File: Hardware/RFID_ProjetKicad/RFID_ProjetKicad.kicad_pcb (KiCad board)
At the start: 2 copper layers, 25 parts, among them J1 TB0011-350-04GR, J2 TB0011-350-04GR, U1 XIAO-ESP32-C6-DIP, U2 CEG006900, U3 MAX3485CSA_T

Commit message: Création du PCB
placement, routage et controle
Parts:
- C2, C3, C4, D1, D2, R2, R3, R4, U3: moved to B.Cu
- L2: value 5 mH -> (none)
- moved E2 134.5 mm to (78.0, 176.0), turned to 90 degrees
- moved D1 134.3 mm to (80.0, 156.0), turned to 180 degrees
- moved F1 131.2 mm to (88.7, 169.4), turned to -90 degrees
- moved C3 127.5 mm to (80.0, 169.5), turned to -90 degrees
- moved C4 120.5 mm to (76.0, 163.5)
- moved D2 113.8 mm to (63.0, 136.0)
- moved R1 106.4 mm to (82.5, 176.0), turned to -90 degrees
- moved J1 105.5 mm to (62.0, 176.0)
- moved C2 99.4 mm to (76.5, 138.5), turned to 90 degrees
- moved J2 95.8 mm to (97.2, 176.5)
- moved R2 93.2 mm to (98.0, 167.0), turned to 180 degrees
- moved L2 87.6 mm to (71.8, 137.3)
- moved PS1 84.5 mm to (77.5, 168.0), turned to 180 degrees
- moved L1 72.4 mm to (101.5, 145.5), turned to 180 degrees
- moved C1 65.0 mm to (63.5, 147.9), turned to 90 degrees
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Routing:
- net GND: track 0.00 -> 749.6 mm, vias 0 -> 1
- net +3V3: track 0.00 -> 394.7 mm, vias 0 -> 3
- net Net-(U1-GPIO21_D3): track 0.00 -> 107.0 mm, vias 0 -> 1
- net /D+: track 0.00 -> 106.4 mm, vias 0 -> 2
- net /D-: track 0.00 -> 106.2 mm, vias 0 -> 2
- net Net-(U1-GPIO16_D6_TX): track 0.00 -> 93.4 mm
- net Net-(U1-GPIO0_A0_D0): track 0.00 -> 92.1 mm
- net +7V à 27.6V: track 0.00 -> 92.0 mm
- net Net-(U1-GPIO20_D9_MISO): track 0.00 -> 81.9 mm
- net Net-(U1-GPIO18_D10_MOSI): track 0.00 -> 76.5 mm
- net Net-(U1-GPIO19_D8_SCK): track 0.00 -> 75.4 mm
- net /SW_COM: track 0.00 -> 70.7 mm, vias 0 -> 2
- net Net-(U1-GPIO17_D7_RX): track 0.00 -> 60.6 mm, vias 0 -> 2
- net Net-(C1-Pad1): track 0.00 -> 53.9 mm
- net +8V à 28V: track 0.00 -> 33.3 mm
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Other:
- board outline added: 72 x 151 mm
- board text added: "+"
- board text added: "+8v-28v"
- board text added: "-"
- board text added: "0v"
- board text added: "D+"
- board text added: "D-"
- board text added: "GND"

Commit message: Correction PCB + Logos
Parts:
- added G***: LOGO, RFID_Empreintes:EST_logo_grand, F.Cu at (50.6, 92.7)
- added G***: LOGO, RFID_Empreintes:QR_GitHub_7mm, F.Cu at (49.6, 127.2)
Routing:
- net Net-(U1-GPIO2_A2_D2): track 2.11 -> 59.4 mm, vias 0 -> 2
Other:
- board text added: "RS485"

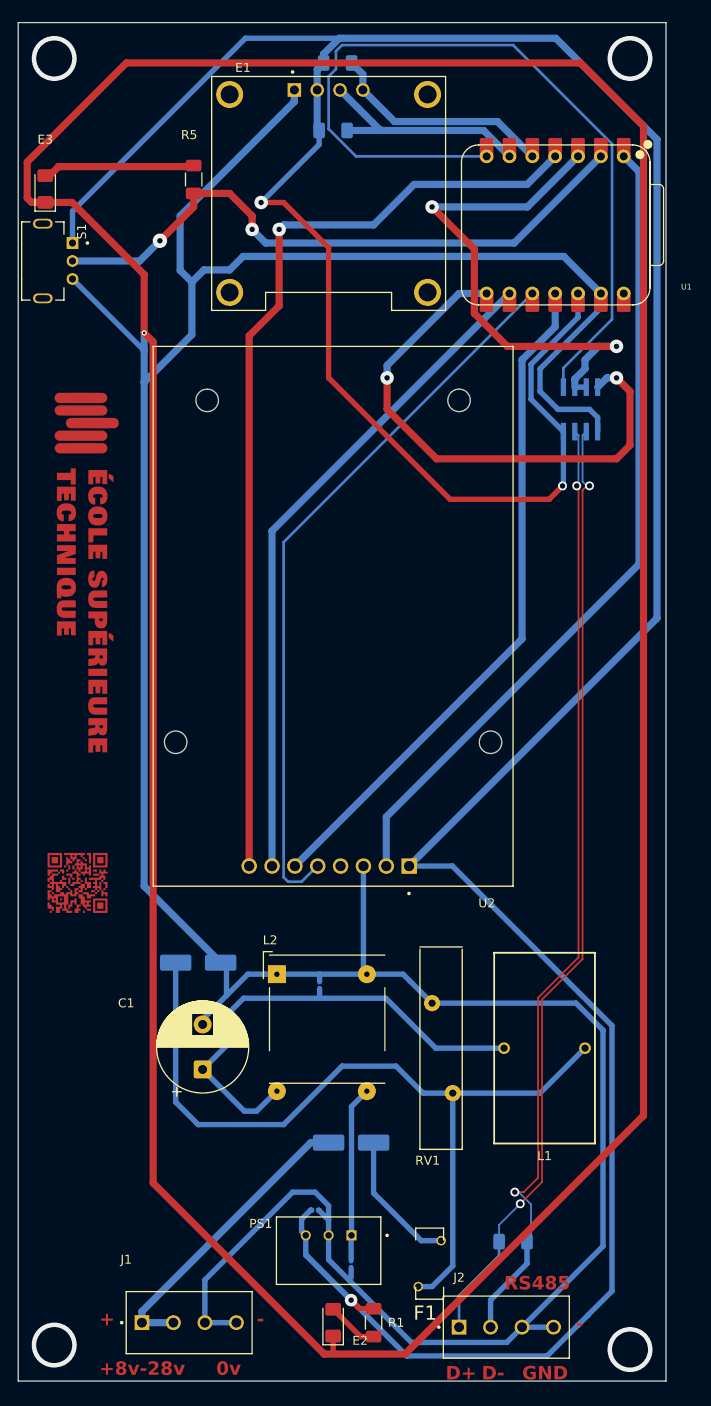
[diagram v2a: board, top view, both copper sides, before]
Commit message: Ajout de points de test sur PCB
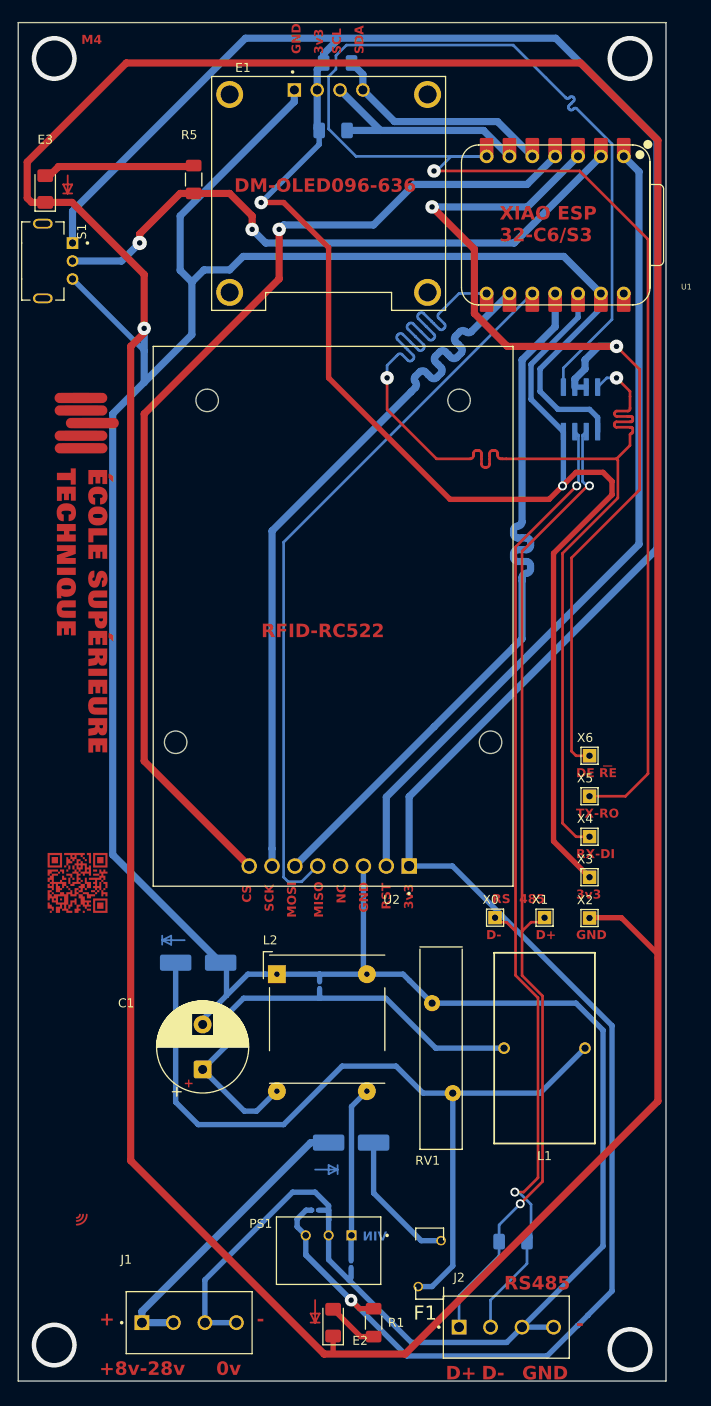
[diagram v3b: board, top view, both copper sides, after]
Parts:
- added X0: , TestPoint:TestPoint_THTPad_1.5x1.5mm_Drill0.7mm, F.Cu at (96.0, 131.0)
- added X1: , TestPoint:TestPoint_THTPad_1.5x1.5mm_Drill0.7mm, F.Cu at (101.5, 131.0)
- added X2: , TestPoint:TestPoint_THTPad_1.5x1.5mm_Drill0.7mm, F.Cu at (106.5, 131.0)
- added X3: , TestPoint:TestPoint_THTPad_1.5x1.5mm_Drill0.7mm, F.Cu at (106.5, 126.5)
- added X4: , TestPoint:TestPoint_THTPad_1.5x1.5mm_Drill0.7mm, F.Cu at (106.5, 122.0)
- added X5: , TestPoint:TestPoint_THTPad_1.5x1.5mm_Drill0.7mm, F.Cu at (106.5, 117.5)
- added X6: , TestPoint:TestPoint_THTPad_1.5x1.5mm_Drill0.7mm, F.Cu at (106.5, 113.0)
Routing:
- net Net-(U1-GPIO16_D6_TX): track 93.4 -> 195.3 mm, vias 0 -> 1
- net Net-(U1-GPIO17_D7_RX): track 60.6 -> 138.2 mm
- net +3V3: track 394.7 -> 450.3 mm
- net Net-(U1-GPIO2_A2_D2): track 59.4 -> 110.8 mm
- net GND: track 749.6 -> 765.4 mm
- net Net-(U1-GPIO21_D3): track 107.0 -> 116.7 mm
- net Net-(U1-GPIO19_D8_SCK): track 75.4 -> 81.8 mm
- net Net-(U1-GPIO18_D10_MOSI): track 76.5 -> 81.8 mm
- net /D+: track 106.4 -> 111.4 mm
- net /D-: track 106.2 -> 111.0 mm
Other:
- board text added: "3v3"
- board text added: "CS"
- board text added: "DE RE"
- board text added: "DM-OLED096-636"
- board text added: "M4"
- board text added: "MISO"
- board text added: "MOSI"
- board text added: "NC"
- board text added: "RFID-RC522"
- board text added: "RS 485"
- board text added: "RST"
- board text added: "RX-DI"
- board text added: "SCK"
- board text added: "SCL"
- board text added: "SDA"
- board text added: "TX-RO"
- board text added: "VIN"
- board text added: "XIAO ESP 32-C6/S3"
- board text added: "_"

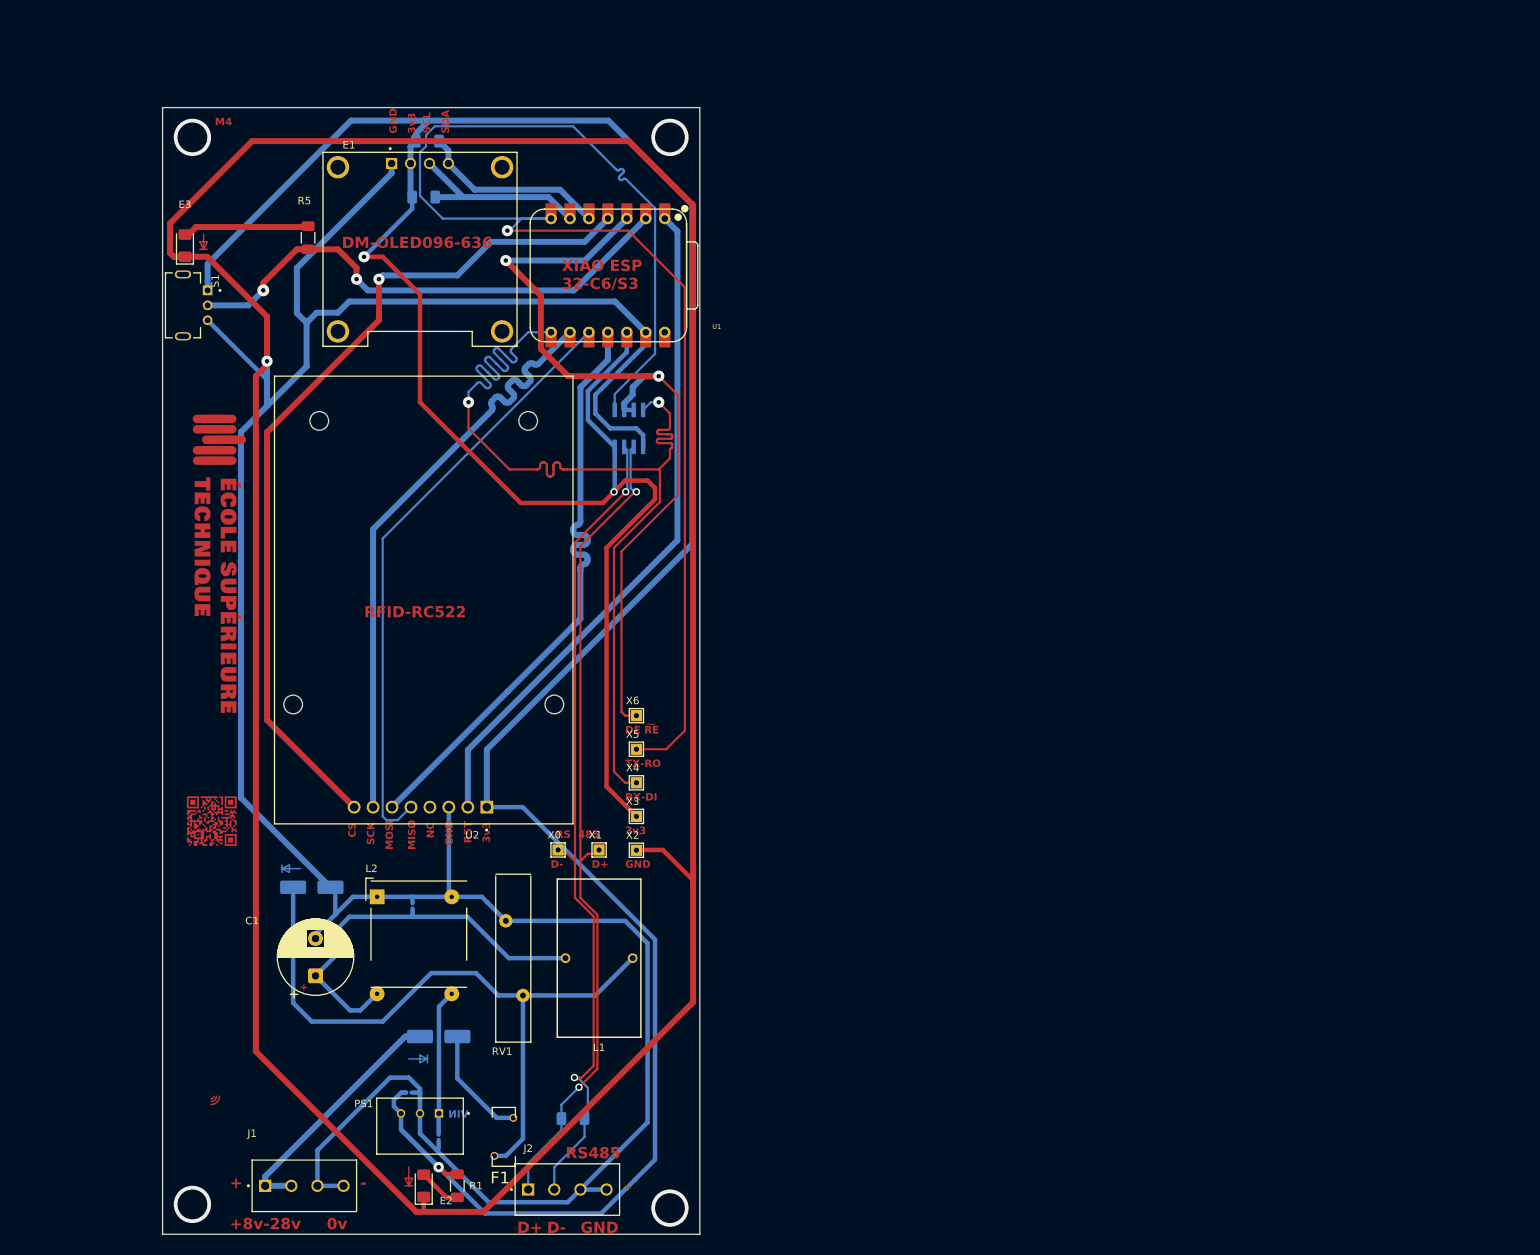
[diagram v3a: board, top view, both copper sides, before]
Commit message: Ajout de la documentation sur l'implémentation PCB + Modification PCB et logos
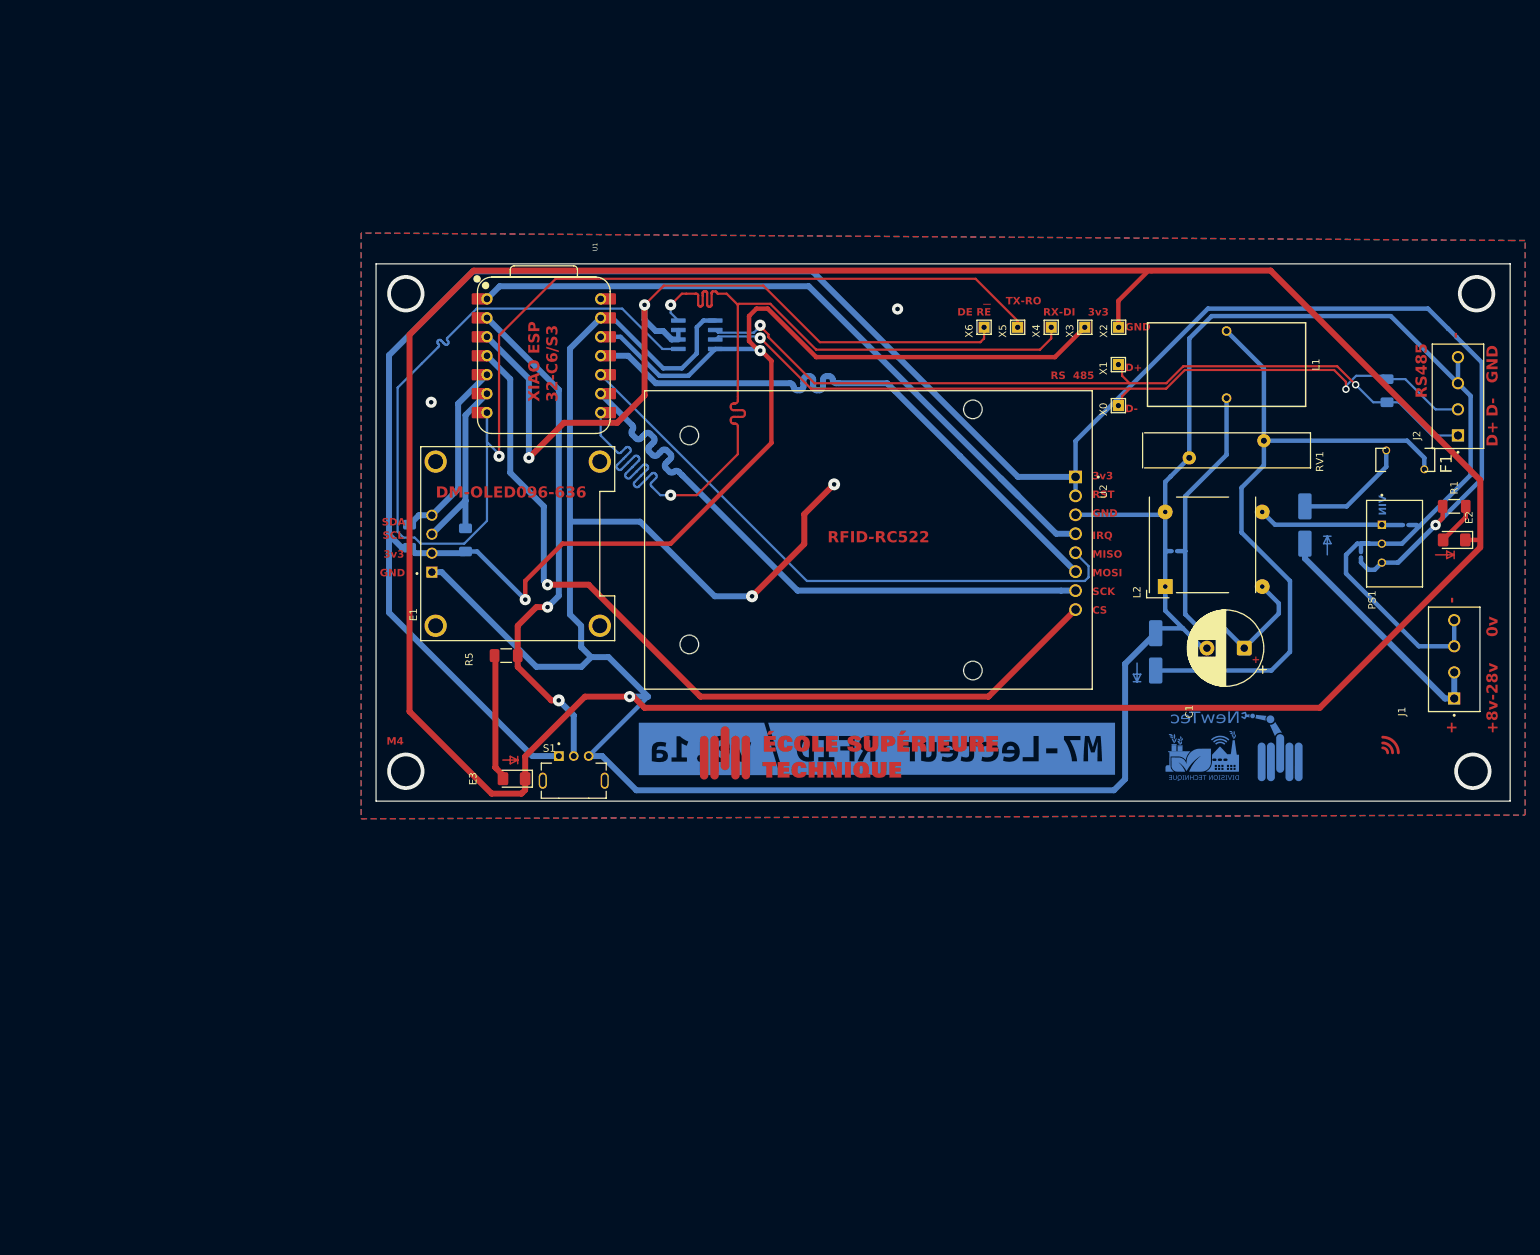
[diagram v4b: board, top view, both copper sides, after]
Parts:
- removed the G*** at (49.6, 127.2)
- added G***: LOGO, RFID_Empreintes:NewTec_logo_20x10_6, B.Cu at (186.5, 117.0)
- added kibuzzard-69FBB450: G***, kibuzzard-69FBB450, B.Cu at (116.3, 117.5)
- added kibuzzard-69FBB4E7: G***, kibuzzard-69FBB4E7, B.Cu at (147.4, 117.4)
- L2: value (none) -> 5 mH
- U2: value CEG006900 -> RFID-RC522
- moved J1 169.5 mm to (216.1, 105.5), turned to 90 degrees
- moved E2 163.0 mm to (216.1, 89.5), turned to 180 degrees
- moved R1 161.7 mm to (216.1, 85.0), turned to 0 degrees
- moved J2 159.8 mm to (216.6, 70.2), turned to 90 degrees
- moved C3 153.4 mm to (209.6, 87.5), turned to 0 degrees
- moved PS1 152.2 mm to (208.1, 90.0), turned to -90 degrees
- moved F1 151.1 mm to (209.5, 78.7), turned to 0 degrees
- moved C4 146.5 mm to (203.6, 91.5), turned to 90 degrees
- moved R2 146.3 mm to (207.1, 69.5), turned to -90 degrees
- moved D1 134.8 mm to (196.1, 87.5), turned to -90 degrees
- moved C1 132.0 mm to (188.0, 104.0), turned to 180 degrees
- moved RV1 124.6 mm to (190.6, 78.5), turned to 180 degrees
- moved D2 117.4 mm to (176.1, 104.5), turned to 90 degrees
- moved L1 115.8 mm to (185.6, 66.0), turned to -90 degrees
- moved L2 113.5 mm to (177.4, 95.7), turned to 90 degrees
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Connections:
- U2 pad 2: Net-(U1-GPIO0_A0_D0) -> +3V3
- U2 pad 4: unconnected-(U2-IRQ-Pad4) -> Net-(U1-GPIO0_A0_D0)
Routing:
- net GND: track 765.4 -> 831.2 mm, vias 1 -> 5
- net Net-(U1-GPIO0_A0_D0): track 92.1 -> 97.5 mm
- net Net-(U1-GPIO16_D6_TX): track 195.3 -> 193.2 mm
- net +3V3: track 450.3 -> 452.4 mm
- net /D+: track 111.4 -> 112.4 mm
- added copper zone on B.Cu, net GND
- added copper zone on F.Cu, net GND
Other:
- board size 72 x 151 mm -> 152 x 72 mm
- board text added: "IRQ"
- board text removed: "NC"

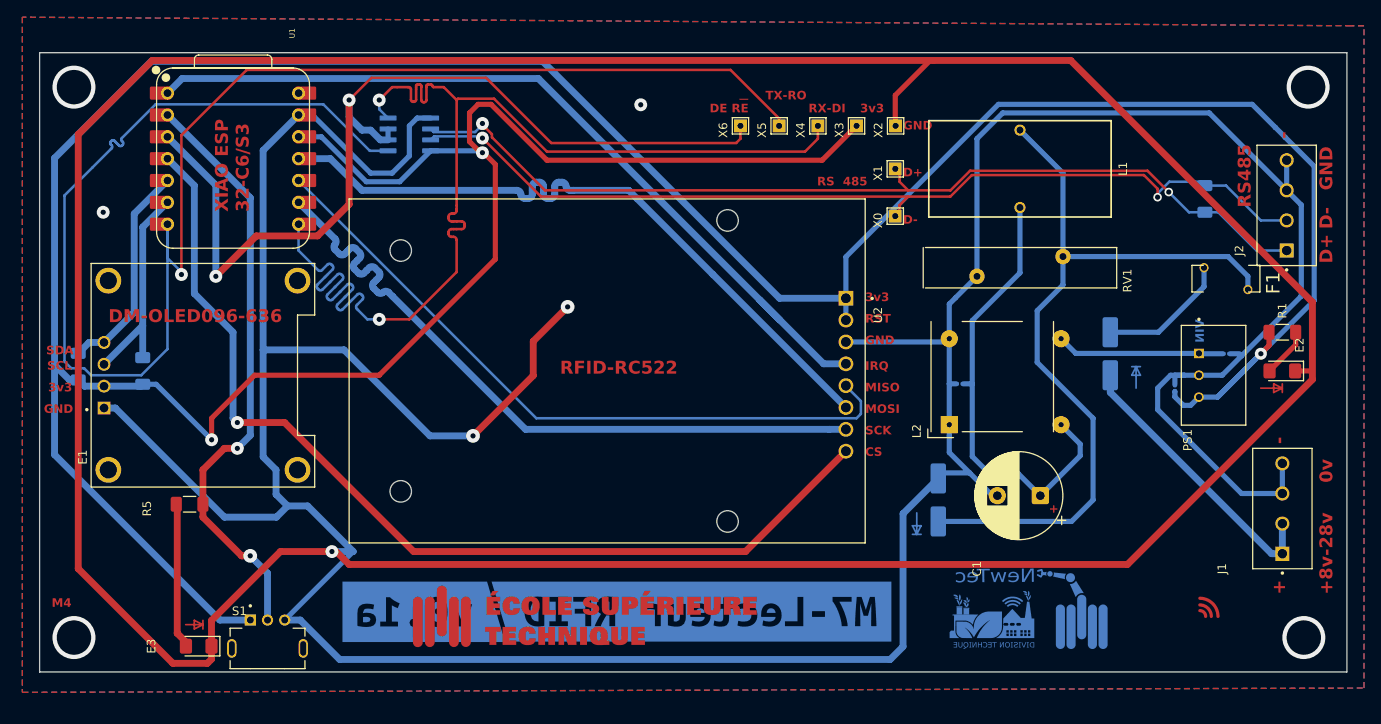
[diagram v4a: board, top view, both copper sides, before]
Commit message: Correction de la violation de la RDC
Modification PCB
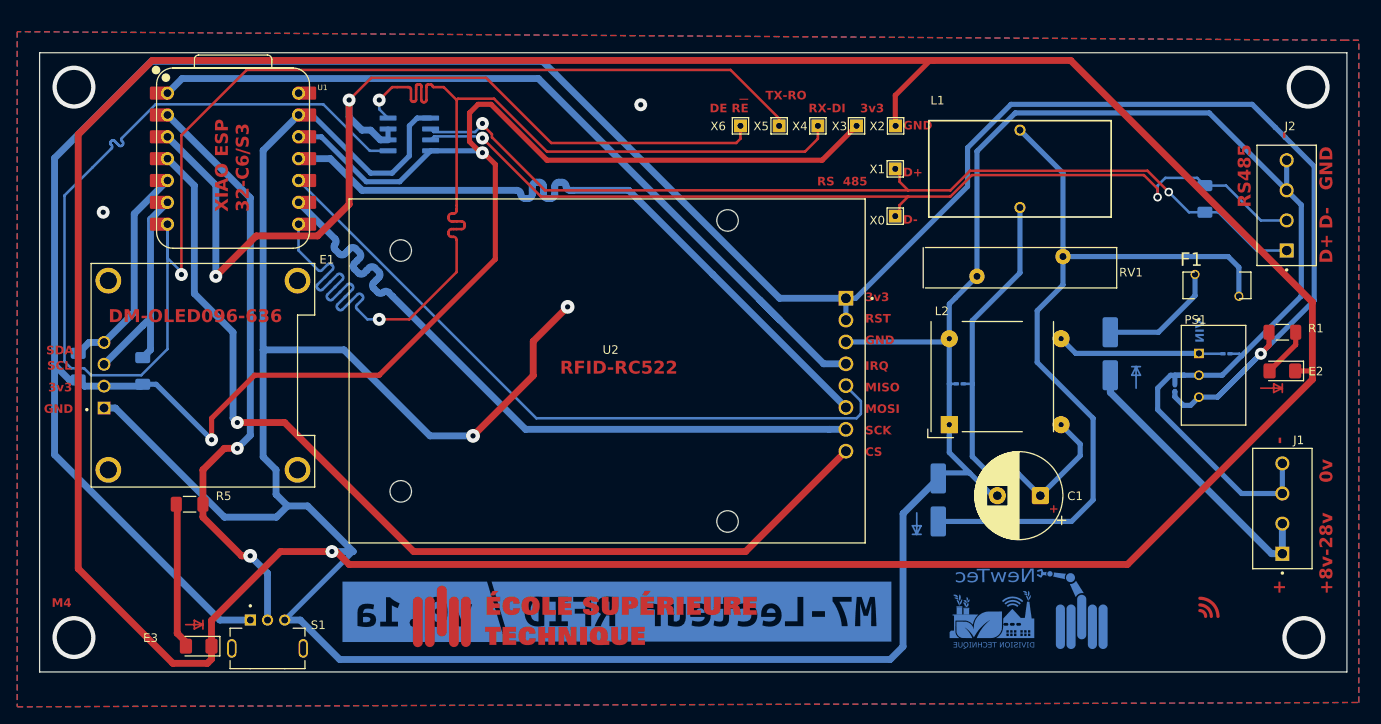
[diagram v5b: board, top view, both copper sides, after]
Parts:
- moved F1 1.30 mm to (208.5, 79.5)
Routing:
- net Net-(D1-K): track 15.3 -> 13.8 mm
- net Net-(E1-SCL): track 26.7 -> 28.0 mm
- net /D-: track 111.0 -> 111.9 mm
- net GND: track 831.2 -> 830.6 mm
